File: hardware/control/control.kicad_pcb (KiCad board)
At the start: 2 copper layers, 110 x 70 mm, 58 parts, among them J1 Conn_01x05_Male, J2 CANPWR, J3 CANGND, J4 RJ45, J5 RJ45, J6 Conn_02x03_Odd_Even, J7 DCDC-PWM, J8 DCDC-MEASURES, J9 display, Q1 BSS123, SW1 next, SW2 select, U1 2.048V, U2 AP63200WU, U3 PIC18F27Q84, U4 TLE9250VSJXUMA1, Y1 10Mhz

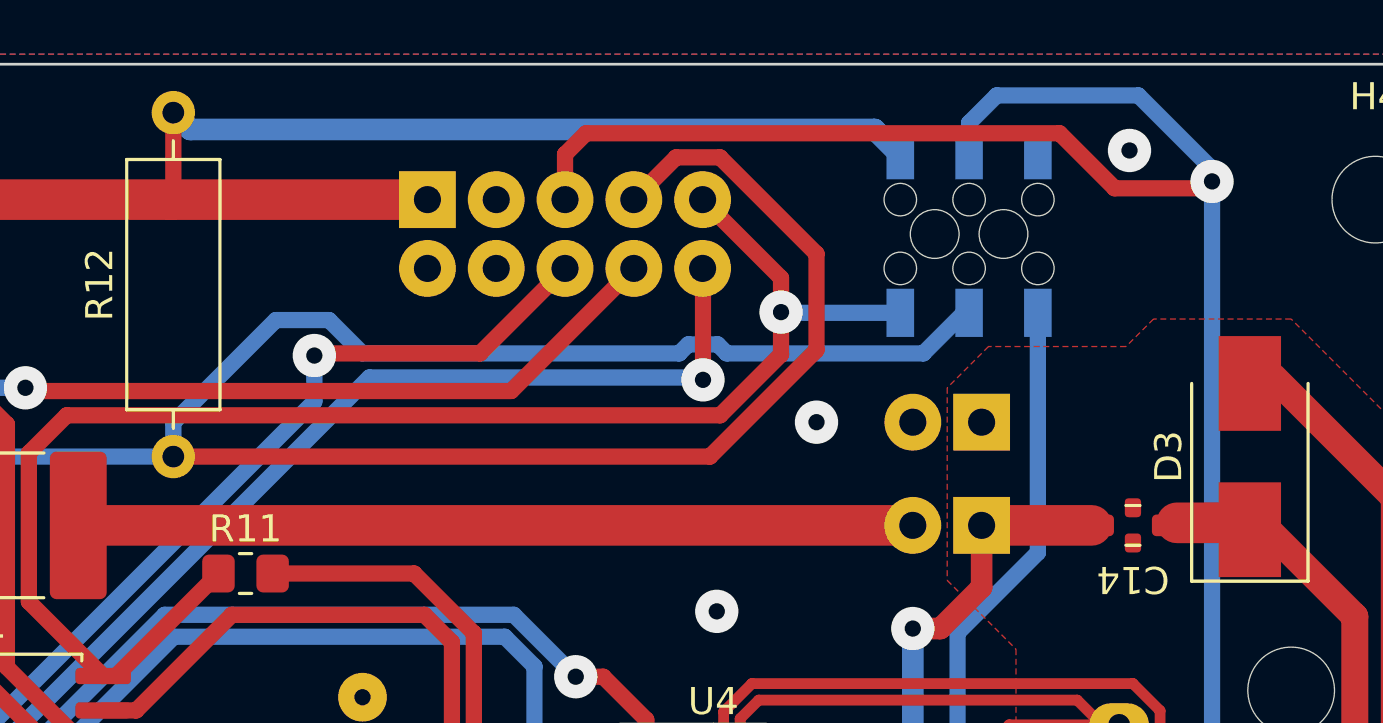
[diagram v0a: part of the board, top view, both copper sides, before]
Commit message: Adjust for "0 height" display nuts
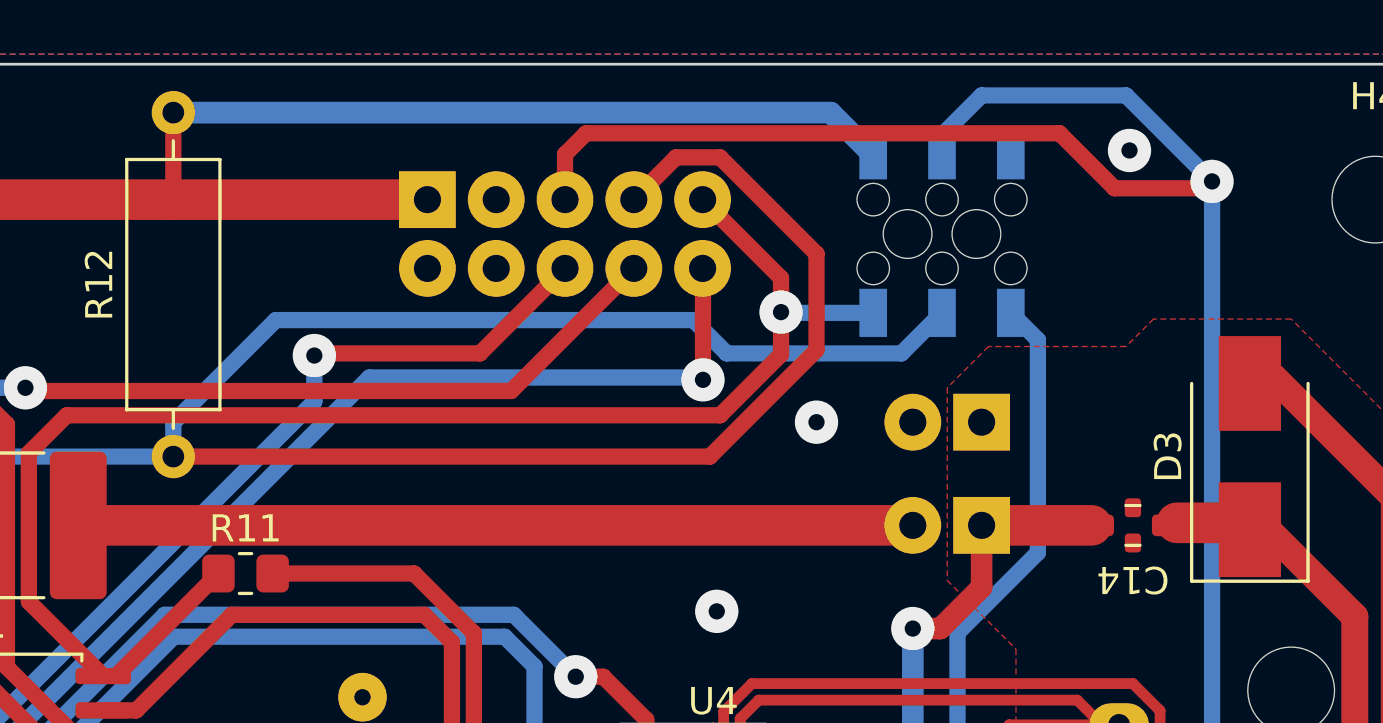
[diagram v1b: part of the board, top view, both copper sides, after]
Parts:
- moved J9 1.00 mm to (139.0, 86.3)
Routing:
- net SDA: track 94.5 -> 93.2 mm
- net SCL: track 55.3 -> 54.3 mm
- net +5V: track 331.2 -> 330.2 mm
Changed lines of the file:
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@@
   )
   (footprint "Connector_Harwin:Harwin_M20-7810345_2x03_P2.54mm_Vertical" locked (layer "B.Cu")
-    (at 140 86.27 -90)
+    (at 139 86.27 -90)
     (descr "Harwin Female Vertical Surface Mount Double Row 2.54mm (0.1 inch) Pitch PCB Connector, M20-7810345, 3 Pins per row (https://cdn.harwin.com/pdfs/M20-781.pdf), generated with kicad-footprint-generator")
     (tags "connector Harwin M20 side entry")
@@
   (segment (start 69.596 90.043) (end 69.596 83.312) (width 1.5) (layer "B.Cu") (net 5))
   (segment (start 113.289 123.983273) (end 113.289 123.439) (width 1.5) (layer "B.Cu") (net 5))
-  (segment (start 137.46 83.36) (end 136.51 82.41) (width 0.8) (layer "B.Cu") (net 5))
   (segment (start 57.404 99.568) (end 60.198 99.568) (width 1.5) (layer "B.Cu") (net 5))
   (segment (start 60.214 102.616) (end 60.214 99.584) (width 1.5) (layer "B.Cu") (net 5))
@@
   (segment (start 113.289 124.403) (end 111.2885 126.4035) (width 1.5) (layer "B.Cu") (net 5))
   (segment (start 75.057 133.897198) (end 75.057 135.509) (width 1.5) (layer "B.Cu") (net 5))
-  (segment (start 136.51 82.41) (end 111.239 82.41) (width 0.8) (layer "B.Cu") (net 5))
   (segment (start 75.1555 133.35) (end 75.1555 130.2125) (width 0.8) (layer "B.Cu") (net 5))
+  (segment (start 136.46 83.36) (end 134.888 81.788) (width 0.8) (layer "B.Cu") (net 5))
   (segment (start 72.009 138.557) (end 57.277 138.557) (width 1.5) (layer "B.Cu") (net 5))
   (segment (start 57.277 138.557) (end 54.61 135.89) (width 1.5) (layer "B.Cu") (net 5))
@@
   (segment (start 75.1555 133.35) (end 75.9275 134.122) (width 1.5) (layer "B.Cu") (net 5))
   (segment (start 75.9275 134.122) (end 99.4695 134.122) (width 1.5) (layer "B.Cu") (net 5))
-  (segment (start 111.239 82.41) (end 110.617 81.788) (width 0.8) (layer "B.Cu") (net 5))
   (segment (start 75.1555 133.798698) (end 75.057 133.897198) (width 1.5) (layer "B.Cu") (net 5))
   (segment (start 122.428 114.3) (end 122.428 113.538) (width 1.5) (layer "B.Cu") (net 5))
   (segment (start 54.61 102.362) (end 57.404 99.568) (width 1.5) (layer "B.Cu") (net 5))
+  (segment (start 134.888 81.788) (end 110.617 81.788) (width 0.8) (layer "B.Cu") (net 5))
   (segment (start 75.057 135.509) (end 72.009 138.557) (width 1.5) (layer "B.Cu") (net 5))
   (segment (start 99.137 126.4035) (end 95.581 126.4035) (width 1.5) (layer "B.Cu") (net 5))
@@
   (segment (start 105.283 94.361) (end 105.283 99.8465) (width 0.6) (layer "F.Cu") (net 14))
   (via (at 133.0565 89.154) (size 1.6) (drill 0.6) (layers "F.Cu" "B.Cu") (net 14))
-  (segment (start 133.0825 89.18) (end 137.46 89.18) (width 0.6) (layer "B.Cu") (net 14))
   (segment (start 133.0565 89.154) (end 133.0825 89.18) (width 0.6) (layer "B.Cu") (net 14))
+  (segment (start 133.0825 89.18) (end 136.46 89.18) (width 0.6) (layer "B.Cu") (net 14))
   (segment (start 130.805174 83.439) (end 134.366 86.999826) (width 0.6) (layer "F.Cu") (net 15))
   (segment (start 129.181 83.439) (end 130.805174 83.439) (width 0.6) (layer "F.Cu") (net 15))
@@
   (segment (start 96.7495 102.5915) (end 98.728 102.5915) (width 0.6) (layer "F.Cu") (net 15))
   (via (at 95.25 101.092) (size 1.6) (drill 0.6) (layers "F.Cu" "B.Cu") (net 15))
+  (segment (start 137.502 90.678) (end 139 89.18) (width 0.6) (layer "B.Cu") (net 15))
+  (segment (start 129.82062 89.4475) (end 131.05112 90.678) (width 0.6) (layer "B.Cu") (net 15))
+  (segment (start 114.40038 89.4475) (end 129.82062 89.4475) (width 0.6) (layer "B.Cu") (net 15))
+  (segment (start 100.457 94.488) (end 110.617 94.488) (width 0.6) (layer "B.Cu") (net 15))
+  (segment (start 131.05112 90.678) (end 137.502 90.678) (width 0.6) (layer "B.Cu") (net 15))
+  (segment (start 95.25 101.092) (end 95.25 99.695) (width 0.6) (layer "B.Cu") (net 15))
+  (segment (start 95.25 99.695) (end 100.457 94.488) (width 0.6) (layer "B.Cu") (net 15))
   (segment (start 110.617 93.23088) (end 114.40038 89.4475) (width 0.6) (layer "B.Cu") (net 15))
-  (segment (start 131.05112 90.678) (end 138.312 90.678) (width 0.6) (layer "B.Cu") (net 15))
-  (segment (start 138.312 90.678) (end 140 88.99) (width 0.6) (layer "B.Cu") (net 15))
-  (segment (start 116.36662 89.4475) (end 117.59712 90.678) (width 0.6) (layer "B.Cu") (net 15))
-  (segment (start 100.457 94.488) (end 110.617 94.488) (width 0.6) (layer "B.Cu") (net 15))
-  (segment (start 129.63238 90.3445) (end 130.71762 90.3445) (width 0.6) (layer "B.Cu") (net 15))
-  (segment (start 95.25 101.092) (end 95.25 99.695) (width 0.6) (layer "B.Cu") (net 15))
-  (segment (start 114.40038 89.4475) (end 116.36662 89.4475) (width 0.6) (layer "B.Cu") (net 15))
-  (segment (start 95.25 99.695) (end 100.457 94.488) (width 0.6) (layer "B.Cu") (net 15))
-  (segment (start 129.29888 90.678) (end 129.63238 90.3445) (width 0.6) (layer "B.Cu") (net 15))
-  (segment (start 117.59712 90.678) (end 129.29888 90.678) (width 0.6) (layer "B.Cu") (net 15))
   (segment (start 110.617 94.488) (end 110.617 93.23088) (width 0.6) (layer "B.Cu") (net 15))
-  (segment (start 130.71762 90.3445) (end 131.05112 90.678) (width 0.6) (layer "B.Cu") (net 15))
   (segment (start 110.630988 118.1265) (end 109.728 117.223512) (width 0.6) (layer "F.Cu") (net 16))
   (segment (start 109.728 113.538) (end 108.966 112.776) (width 0.6) (layer "F.Cu") (net 16))
@@
   (via (at 125.222 120.396) (size 1.6) (drill 0.6) (layers "F.Cu" "B.Cu") (net 16))
   (segment (start 131.187957 114.530853) (end 132.305473 114.530853) (width 0.6) (layer "B.Cu") (net 16))
+  (segment (start 125.222 120.396) (end 125.32281 120.396) (width 0.6) (layer "B.Cu") (net 16))
+  (segment (start 125.32281 120.396) (end 131.187957 114.530853) (width 0.6) (layer "B.Cu") (net 16))
+  (segment (start 139.573 107.263326) (end 139.573 101.001) (width 0.6) (layer "B.Cu") (net 16))
+  (segment (start 142.54 98.034) (end 142.54 90.18) (width 0.6) (layer "B.Cu") (net 16))
+  (segment (start 132.305473 114.530853) (end 139.573 107.263326) (width 0.6) (layer "B.Cu") (net 16))
+  (segment (start 142.54 90.18) (end 141.54 89.18) (width 0.6) (layer "B.Cu") (net 16))
   (segment (start 139.573 101.001) (end 142.54 98.034) (width 0.6) (layer "B.Cu") (net 16))
-  (segment (start 139.573 107.263326) (end 139.573 101.001) (width 0.6) (layer "B.Cu") (net 16))
-  (segment (start 125.32281 120.396) (end 131.187957 114.530853) (width 0.6) (layer "B.Cu") (net 16))
-  (segment (start 132.305473 114.530853) (end 139.573 107.263326) (width 0.6) (layer "B.Cu") (net 16))
-  (segment (start 125.222 120.396) (end 125.32281 120.396) (width 0.6) (layer "B.Cu") (net 16))
-  (segment (start 142.54 98.034) (end 142.54 89.18) (width 0.6) (layer "B.Cu") (net 16))
   (segment (start 137.922 97.028) (end 107.107 97.028) (width 1.5) (layer "F.Cu") (net 17))
   (segment (start 71.882 95.077) (end 65.083 95.077) (width 1.5) (layer "F.Cu") (net 18))
@@
   (via (at 148.971 84.328) (size 1.6) (drill 0.6) (layers "F.Cu" "B.Cu") (net 52))
   (via (at 129.286 121.666) (size 1.6) (drill 0.6) (layers "F.Cu" "B.Cu") (net 52))
-  (segment (start 148.971 84.328) (end 148.971 83.87238) (width 0.6) (layer "B.Cu") (net 52))
-  (segment (start 148.971 83.87238) (end 146.25162 81.153) (width 0.6) (layer "B.Cu") (net 52))
-  (segment (start 146.25162 81.153) (end 141.017 81.153) (width 0.6) (layer "B.Cu") (net 52))
   (segment (start 134.62 116.332) (end 145.415 116.332) (width 0.6) (layer "B.Cu") (net 52))
   (segment (start 148.971 112.776) (end 148.971 84.328) (width 0.6) (layer "B.Cu") (net 52))
-  (segment (start 140 82.17) (end 140 83.36) (width 0.6) (layer "B.Cu") (net 52))
+  (segment (start 148.971 84.328) (end 145.796 81.153) (width 0.6) (layer "B.Cu") (net 52))
+  (segment (start 139 82.615) (end 139 83.36) (width 0.6) (layer "B.Cu") (net 52))
   (segment (start 129.286 121.666) (end 134.62 116.332) (width 0.6) (layer "B.Cu") (net 52))
-  (segment (start 141.017 81.153) (end 140 82.17) (width 0.6) (layer "B.Cu") (net 52))
+  (segment (start 140.462 81.153) (end 139 82.615) (width 0.6) (layer "B.Cu") (net 52))
+  (segment (start 145.796 81.153) (end 140.462 81.153) (width 0.6) (layer "B.Cu") (net 52))
   (segment (start 145.415 116.332) (end 148.971 112.776) (width 0.6) (layer "B.Cu") (net 52))
   (segment (start 115.824 90.7575) (end 115.9035 90.678) (width 0.6) (layer "F.Cu") (net 53))

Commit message: One more cosmetic track adjust
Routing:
- net +5V: track 330.2 -> 328.5 mm
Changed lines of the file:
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@@
   (segment (start 111.252 108.9415) (end 113.03 110.7195) (width 0.6) (layer "F.Cu") (net 4))
   (segment (start 108.028 108.9415) (end 111.252 108.9415) (width 0.6) (layer "F.Cu") (net 4))
-  (segment (start 101.346 128.899976) (end 102.398024 129.952) (width 0.6) (layer "F.Cu") (net 5))
   (segment (start 69.812 83.274) (end 96.231909 83.274) (width 1.5) (layer "F.Cu") (net 5))
   (segment (start 98.728 108.9415) (end 95.5255 108.9415) (width 0.6) (layer "F.Cu") (net 5))
+  (segment (start 98.728 108.9415) (end 99.5435 108.9415) (width 0.6) (layer "F.Cu") (net 5))
   (segment (start 69.596 90.043) (end 65.037 90.043) (width 1.5) (layer "F.Cu") (net 5))
   (segment (start 114.284 98.806) (end 119.509513 98.806) (width 0.6) (layer "F.Cu") (net 5))
   (segment (start 133.031 108.839) (end 130.937 108.839) (width 0.6) (layer "F.Cu") (net 5))
+  (segment (start 100.33 109.728) (end 100.33 127.883976) (width 0.6) (layer "F.Cu") (net 5))
   (segment (start 123.4225 107.4635) (end 125.222 107.4635) (width 1.5) (layer "F.Cu") (net 5))
   (segment (start 122.428 113.538) (end 122.428 111.49) (width 1.5) (layer "F.Cu") (net 5))
@@
   (segment (start 113.289 124.403) (end 113.289 121.671) (width 0.6) (layer "F.Cu") (net 5))
   (segment (start 110.617 81.788) (end 110.617 84.91) (width 0.6) (layer "F.Cu") (net 5))
-  (segment (start 102.398024 129.952) (end 110.528976 129.952) (width 0.6) (layer "F.Cu") (net 5))
   (segment (start 122.428 111.49) (end 122.19 111.252) (width 1.5) (layer "F.Cu") (net 5))
   (segment (start 122.19 111.252) (end 122.19 108.696) (width 1.5) (layer "F.Cu") (net 5))
   (segment (start 113.046 121.428) (end 113.8545 121.428) (width 0.6) (layer "F.Cu") (net 5))
   (segment (start 121.714 101.010487) (end 121.714 105.755) (width 0.6) (layer "F.Cu") (net 5))
-  (segment (start 113.289 127.191976) (end 113.289 124.403) (width 0.6) (layer "F.Cu") (net 5))
-  (segment (start 110.528976 129.952) (end 113.289 127.191976) (width 0.6) (layer "F.Cu") (net 5))
+  (segment (start 102.398024 129.952) (end 107.74 129.952) (width 0.6) (layer "F.Cu") (net 5))
   (segment (start 110.527 85) (end 120 85) (width 1.5) (layer "F.Cu") (net 5))
+  (segment (start 100.33 127.883976) (end 102.398024 129.952) (width 0.6) (layer "F.Cu") (net 5))
   (segment (start 121.714 105.755) (end 123.4225 107.4635) (width 0.6) (layer "F.Cu") (net 5))
+  (segment (start 107.74 129.952) (end 113.289 124.403) (width 0.6) (layer "F.Cu") (net 5))
   (segment (start 122.19 108.696) (end 123.4225 107.4635) (width 1.5) (layer "F.Cu") (net 5))
-  (segment (start 101.346 110.744) (end 101.346 128.899976) (width 0.6) (layer "F.Cu") (net 5))
   (segment (start 110.617 84.91) (end 110.527 85) (width 0.6) (layer "F.Cu") (net 5))
-  (segment (start 98.728 108.9415) (end 99.5435 108.9415) (width 0.6) (layer "F.Cu") (net 5))
   (segment (start 129.667 107.569) (end 128.081 107.569) (width 0.6) (layer "F.Cu") (net 5))
-  (segment (start 99.5435 108.9415) (end 101.346 110.744) (width 0.6) (layer "F.Cu") (net 5))
+  (segment (start 99.5435 108.9415) (end 100.33 109.728) (width 0.6) (layer "F.Cu") (net 5))
   (segment (start 113.014 121.428) (end 110.871 121.428) (width 0.6) (layer "F.Cu") (net 5))
   (segment (start 125.222 107.4635) (end 127.9755 107.4635) (width 0.6) (layer "F.Cu") (net 5))

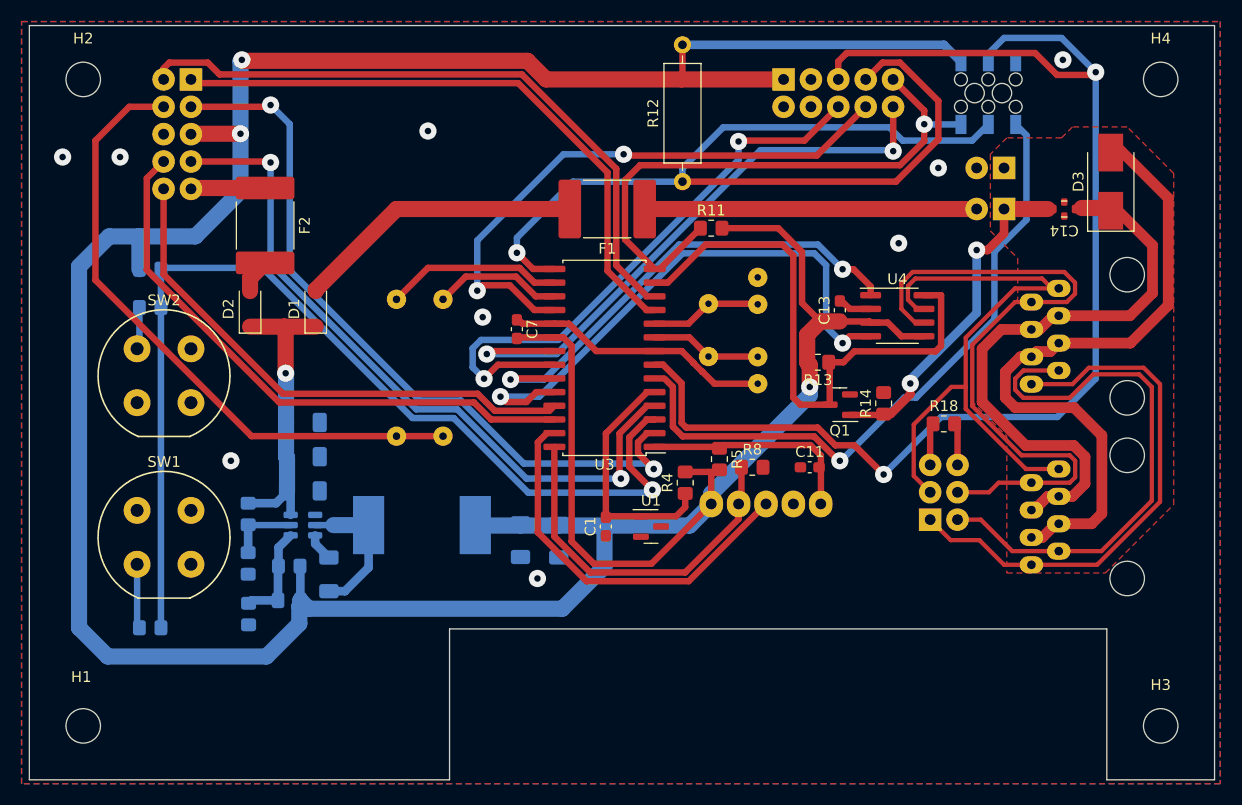
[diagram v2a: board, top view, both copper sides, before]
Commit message: On second though, the pac1953  won't be fast enough for the PWM regulation loop. So add a resistor divider routed to RA5 to get the solar voltage from the PIC18's ADC.
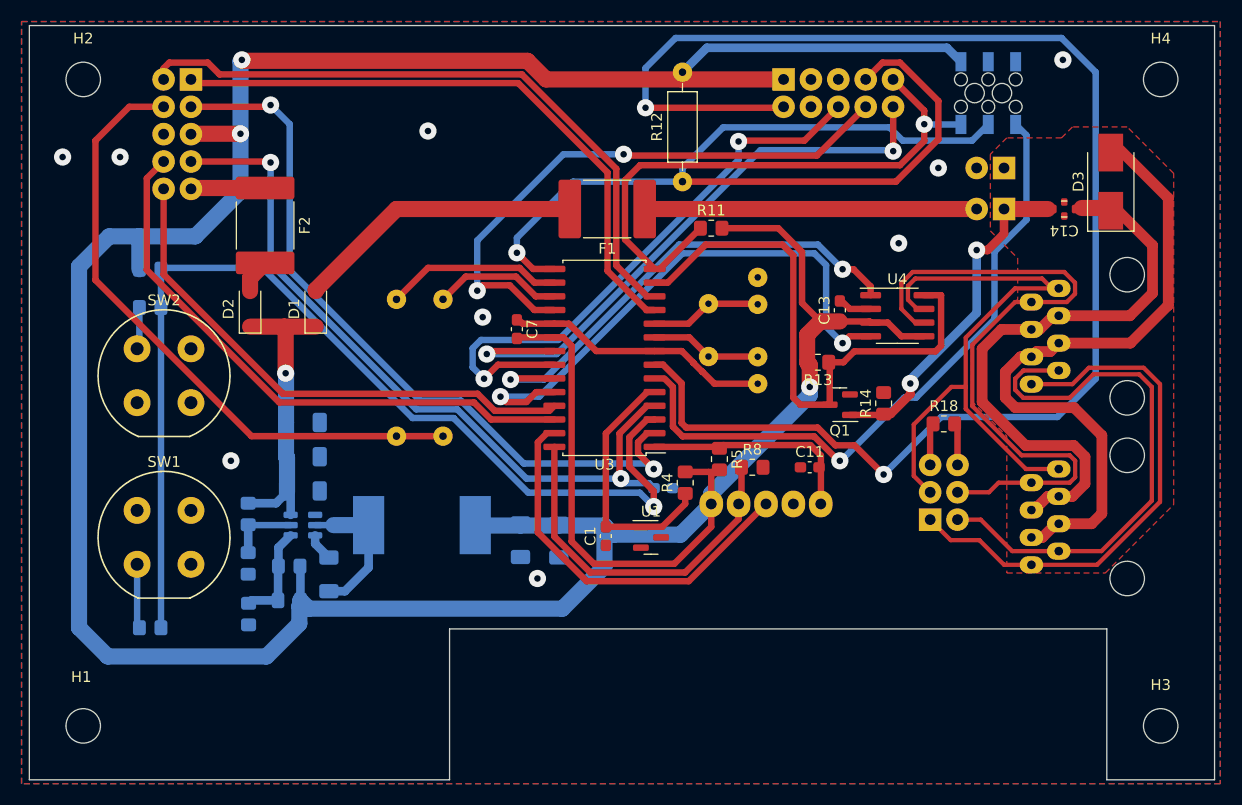
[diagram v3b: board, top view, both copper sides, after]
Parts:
- added C15: 100nF, Capacitor_SMD:C_0603_1608Metric_Pad1.08x0.95mm_HandSolder, B.Cu at (108.8, 122.9)
- R12: footprint Resistor_THT:R_Axial_DIN0309_L9.0mm_D3.2mm_P12.70mm_Horizontal -> Resistor_THT:R_Axial_DIN0207_L6.3mm_D2.5mm_P10.16mm_Horizontal
- moved U1 1.02 mm to (107.7, 127.5)
- moved C1 0.89 mm to (103.5, 127.4)
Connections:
- J7 pad 7: TH -> Solar_V
- J8 pad 2: unconnected-(J8-Pad2) -> TH
- J8 pad 5: RA5 -> unconnected-(J8-Pad5)
- J9 pad 2: RA5 -> unconnected-(J9-Pad2)
- U3 pad 4: TH -> Solar_V
- U3 pad 7: RA5 -> TH
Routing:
- net RA5: track 118.9 -> 0.00 mm, vias 2 -> 0
- net TH: track 65.5 -> 140.1 mm
- net Solar_V: track 0.00 -> 68.9 mm, vias 0 -> 2
- net BTN_IN: track 96.3 -> 98.5 mm
- net Net-(C1-Pad2): track 21.9 -> 23.3 mm
